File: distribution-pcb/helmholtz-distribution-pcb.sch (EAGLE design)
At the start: 34 parts

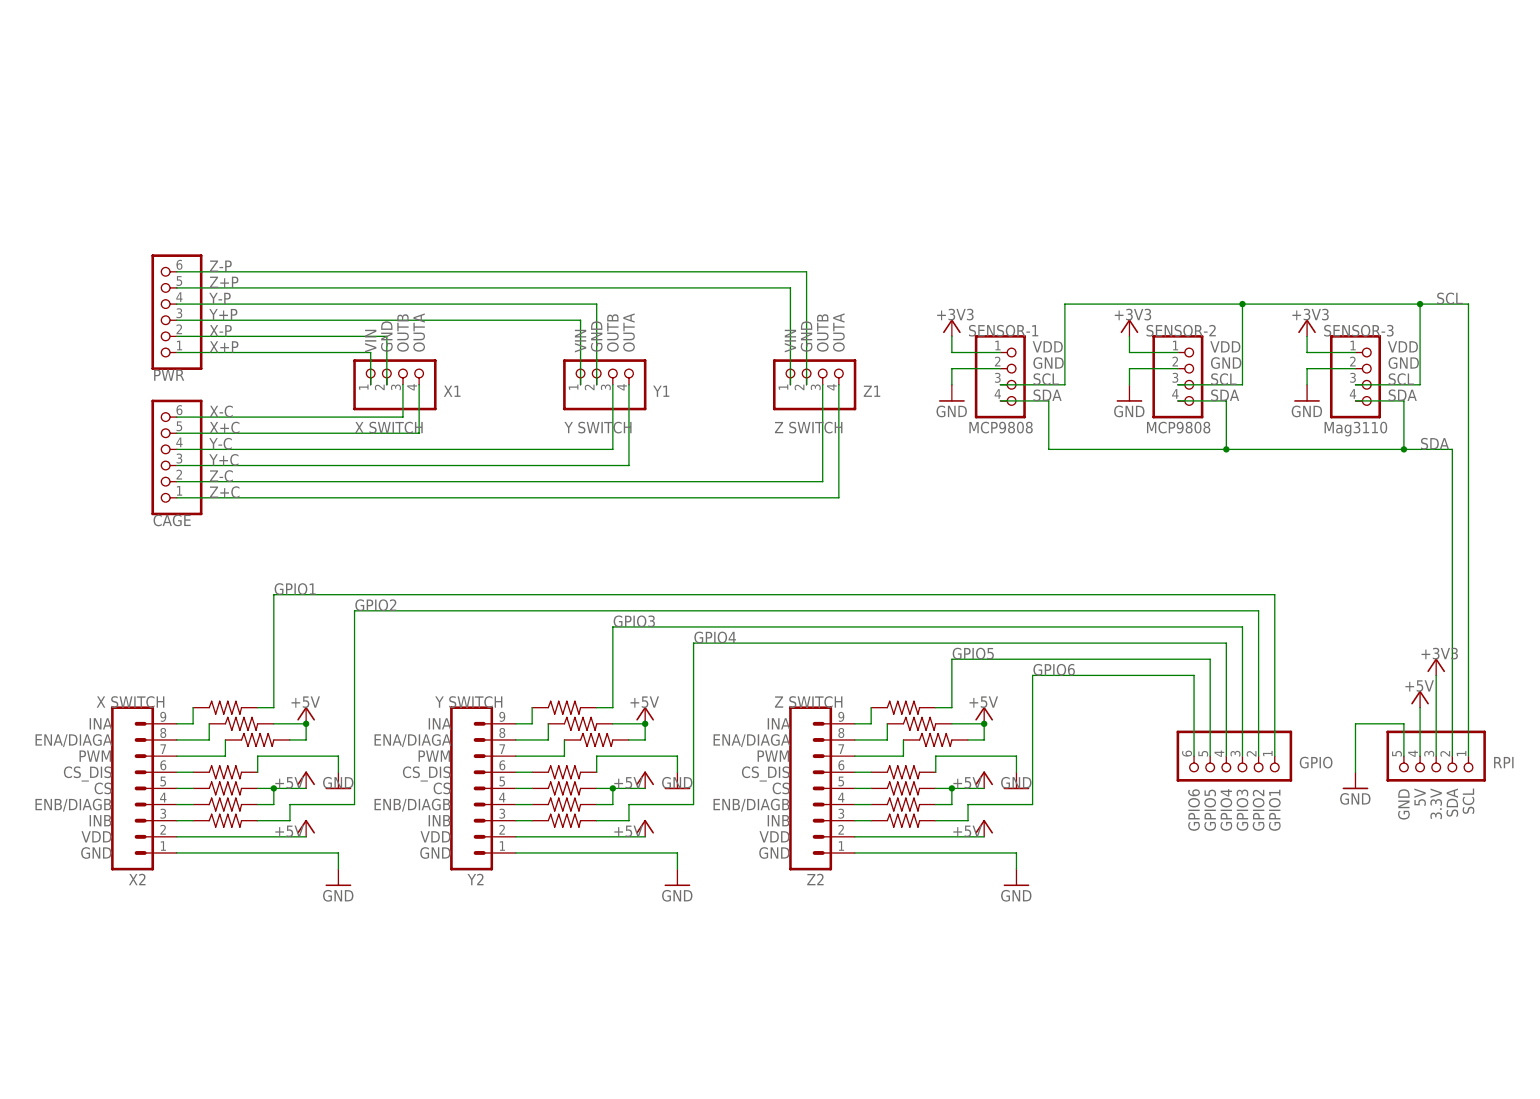
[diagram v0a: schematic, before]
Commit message: Latest distribution PCB design by Ceasar.
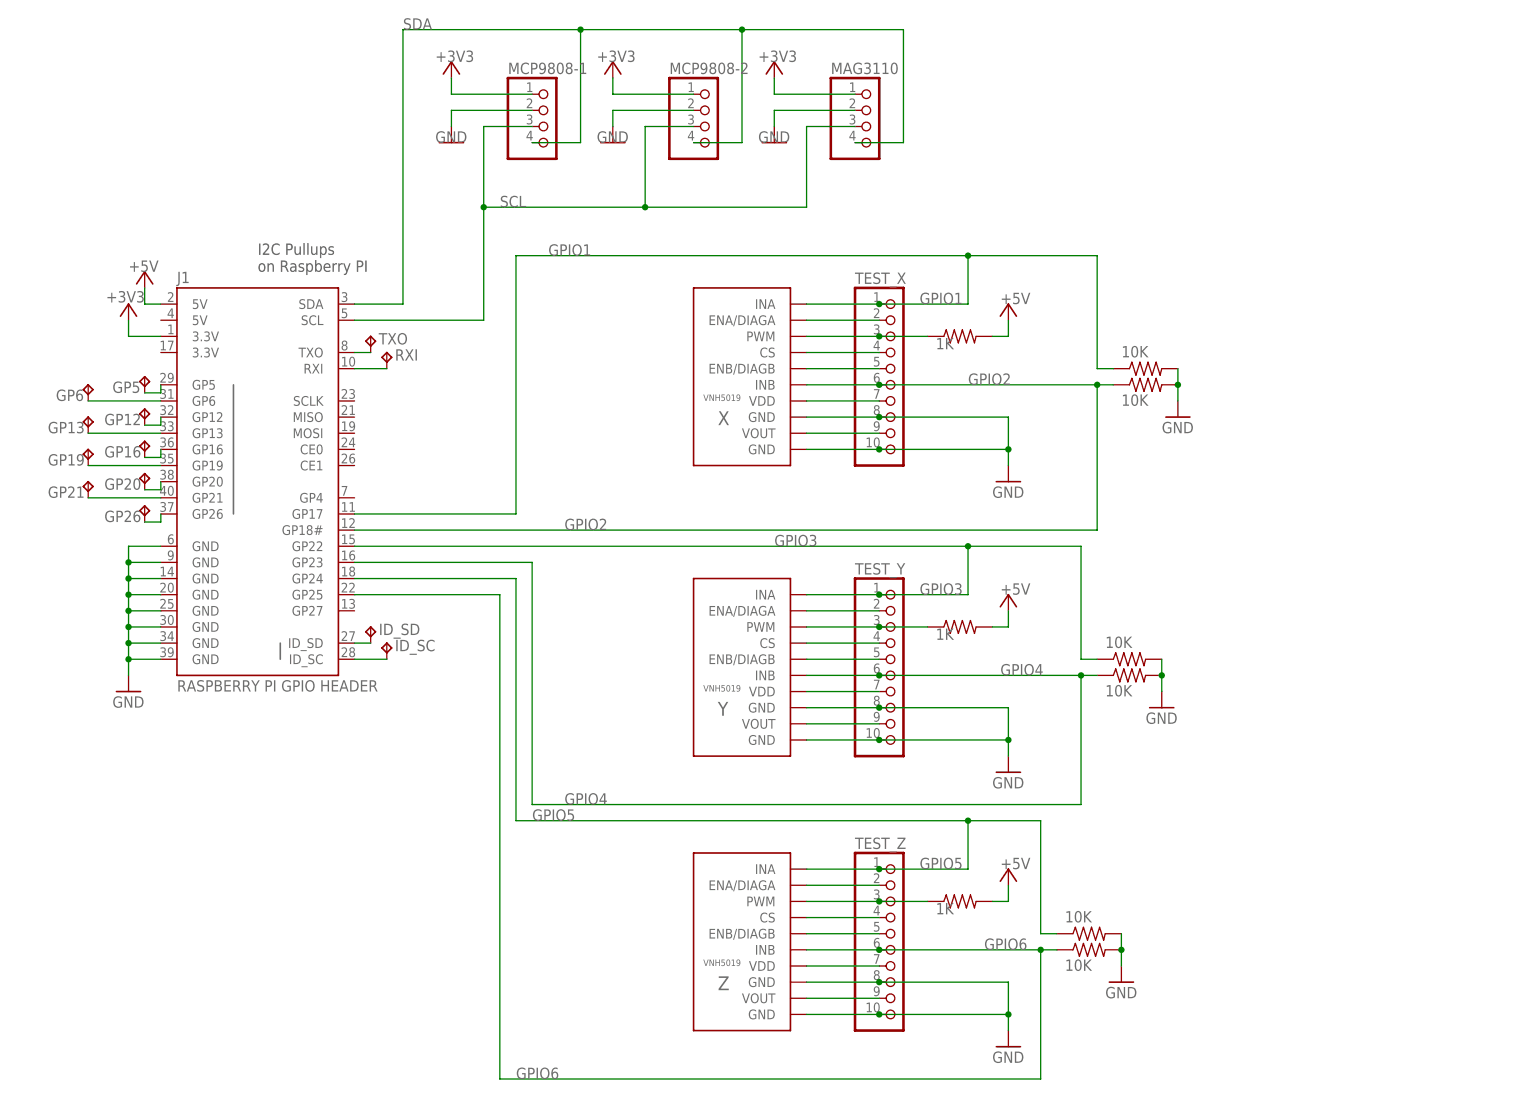
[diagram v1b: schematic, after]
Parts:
- removed CAGE, GPIO, PWR: (no value), pinhead:PINHD-1X6
- removed R1, R11, R12, R14, R15, R18, R19, R21, R4, R5, R6, R8: (no value), rcl:R-US_0204/7
- removed RPI: (no value), pinhead:PINHD-1X5
- removed SENSOR-1, SENSOR-2, SENSOR-3, X1, Y1, Z1: (no value), pinhead:PINHD-1X4
- removed X2, Y2, Z2: (no value), SparkFun-Connectors:CONN_09
- added GP12, GP13, GP16, GP19, GP20, GP21, GP26, GP5, GP6, ID_SC, ID_SD, RXI, TXO: TPPAD1-13, testpad:TPPAD1-13
- added J1: RASPBERRYPI-40-PIN-GPIO_PTH, SparkFun-Connectors:RASPBERRYPI-40-PIN-GPIO_PTH
- added MAG3110, MCP9808-1, MCP9808-2: (no value), pinhead:PINHD-1X4
- added TEST_X, TEST_Y, TEST_Z: (no value), pinhead:PINHD-1X10
- added X, Y, Z: VNH5019, HelmholtzCage:VNH5019
- R10, R16, R17, R2, R3, R9: value (none) -> 10K; device rcl:R-US_0204/7 -> rcl:R-US_R0603
- R13, R20, R7: value (none) -> 1K; device rcl:R-US_0204/7 -> rcl:R-US_R0603
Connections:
- removed net CSX: R7.1, X2.5
- removed net CSY: R8.1, Y2.5
- removed net CSZ: R21.1, Z2.5
- removed net DISX: R6.1, X2.6
- removed net DISY: R9.1, Y2.6
- removed net DISZ: R20.1, Z2.6
- removed net ENAX: R3.1, X2.8
- removed net ENAY: R12.1, Y2.8
- removed net ENAZ: R17.1, Z2.8
- removed net ENBX: R4.1, X2.4
- removed net ENBY: R11.1, Y2.4
- removed net ENBZ: R18.1, Z2.4
- removed net PWMX: R5.1, X2.7
- removed net PWMY: R10.1, Y2.7
- removed net PWMZ: R19.1, Z2.7
- removed net RGP1: R1.1, X2.9
- removed net RGP2: R2.1, X2.3
- removed net RGP3: R14.1, Y2.9
- removed net RGP4: R13.1, Y2.3
- removed net RGP5: R15.1, Z2.9
- removed net RGP6: R16.1, Z2.3
- removed net X+C: CAGE.5, X1.4
- removed net X+P: PWR.1, X1.1
- removed net X-C: CAGE.6, X1.3
- removed net X-P: PWR.2, X1.2
- removed net Y+C: CAGE.3, Y1.4
- removed net Y+P: PWR.3, Y1.1
- removed net Y-C: CAGE.4, Y1.3
- removed net Y-P: PWR.4, Y1.2
- removed net Z+C: CAGE.1, Z1.4
- removed net Z+P: PWR.5, Z1.1
- removed net Z-C: CAGE.2, Z1.3
- removed net Z-P: PWR.6, Z1.2
- new net CS_X: TEST_X.4, X.CS
- new net CS_Y: TEST_Y.4, Y.CS
- new net CS_Z: TEST_Z.4, Z.CS
- new net ENA/DIAGA_X: TEST_X.2, X.ENA/DIAGA
- new net ENA/DIAGA_Y: TEST_Y.2, Y.ENA/DIAGA
- new net ENA/DIAGA_Z: TEST_Z.2, Z.ENA/DIAGA
- new net ENB/DIAGB_X: TEST_X.5, X.ENB/DIAGB
- new net ENB/DIAGB_Y: TEST_Y.5, Y.ENB/DIAGB
- new net ENB/DIAGB_Z: TEST_Z.5, Z.ENB/DIAGB
- new net N$1: GP26.TP, J1.GP26
- new net N$10: J1.TXO, TXO.TP
- new net N$11: J1.RXI, RXI.TP
- new net N$12: ID_SD.TP, J1.ID_SD
- new net N$13: ID_SC.TP, J1.ID_SC
- new net N$2: GP21.TP, J1.GP21
- new net N$3: GP20.TP, J1.GP20
- new net N$4: GP19.TP, J1.GP19
- new net N$5: GP16.TP, J1.GP16
- new net N$6: GP13.TP, J1.GP13
- new net N$7: GP12.TP, J1.GP12
- new net N$8: GP6.TP, J1.GP6
- new net N$9: GP5.TP, J1.GP5
- new net PWM_X: R20.1, TEST_X.3, X.PWM
- new net PWM_Y: R13.1, TEST_Y.3, Y.PWM
- new net PWM_Z: R7.1, TEST_Z.3, Z.PWM
- new net VDD_X: TEST_X.7, X.VDD
- new net VDD_Y: TEST_Y.7, Y.VDD
- new net VDD_Z: TEST_Z.7, Z.VDD
- new net VOUT_X: TEST_X.9, X.VOUT
- new net VOUT_Y: TEST_Y.9, Y.VOUT
- new net VOUT_Z: TEST_Z.9, Z.VOUT
- net +3V3: now also J1.3.3V@1, MAG3110.1, MCP9808-1.1, MCP9808-2.1; no longer RPI.3, SENSOR-1.1, SENSOR-2.1, SENSOR-3.1
- net +5V: now also J1.5V@2, R13.2, R20.2; no longer R10.2, R11.2, R12.2, R17.2, R18.2, R19.2, R21.2, R3.2, R4.2, R5.2, R8.2, RPI.4, X2.2, Y2.2, Z2.2
- net GND: now also J1.GND@14, J1.GND@20, J1.GND@25, J1.GND@30, J1.GND@34, J1.GND@39, J1.GND@6, J1.GND@9, MAG3110.2, MCP9808-1.2, MCP9808-2.2, R10.2, R16.2, R17.2, R2.2, R3.2, TEST_X.10, TEST_X.8, TEST_Y.10, TEST_Y.8, TEST_Z.10, TEST_Z.8, X.GND@1, X.GND@2, Y.GND@1, Y.GND@2, Z.GND@1, Z.GND@2; no longer R20.2, R6.2, RPI.5, SENSOR-1.2, SENSOR-2.2, SENSOR-3.2, X2.1, Y2.1, Z2.1
- net GPIO1: now also J1.GP17, R17.1, TEST_X.1, X.INA; no longer GPIO.1, R1.2
- net GPIO2: now also J1.GP18#, R16.1, TEST_X.6, X.INB; no longer GPIO.2, R2.2
- net GPIO3: now also J1.GP22, R10.1, TEST_Y.1, Y.INA; no longer GPIO.3, R14.2
- net GPIO4: now also J1.GP23, R9.1, TEST_Y.6, Y.INB; no longer GPIO.4, R13.2
- net GPIO5: now also J1.GP24, R3.1, TEST_Z.1, Z.INA; no longer GPIO.5, R15.2
- net GPIO6: now also J1.GP25, R2.1, TEST_Z.6, Z.INB; no longer GPIO.6, R16.2
- net SCL: now also J1.SCL, MAG3110.3, MCP9808-1.3, MCP9808-2.3; no longer RPI.1, SENSOR-1.3, SENSOR-2.3, SENSOR-3.3
- net SDA: now also J1.SDA, MAG3110.4, MCP9808-1.4, MCP9808-2.4; no longer RPI.2, SENSOR-1.4, SENSOR-2.4, SENSOR-3.4
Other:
- note added: "I2C Pullups on Raspberry PI"
- note added: "RASPBERRY PI GPIO HEADER"
- note added: "X"
- note added: "Y"
- note added: "Z"
- note removed: "3.3V"
- note removed: "5V"
- note removed: "CS"
- note removed: "CS_DIS"
- note removed: "ENA/DIAGA"
- note removed: "ENB/DIAGB"
- note removed: "GND"
- note removed: "GPIO1"
- note removed: "GPIO2"
- note removed: "GPIO3"
- note removed: "GPIO4"
- note removed: "GPIO5"
- note removed: "GPIO6"
- note removed: "INA"
- note removed: "INB"
- note removed: "MCP9808"
- note removed: "Mag3110"
- note removed: "OUTA"
- note removed: "OUTB"
- note removed: "PWM"
- note removed: "SCL"
- note removed: "SDA"
- note removed: "VDD"
- note removed: "VIN"
- note removed: "X SWITCH"
- note removed: "Y SWITCH"
- note removed: "Z SWITCH"

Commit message: Added mounting holes to VNH boards, put mounting holes on board, and changed font to vector.
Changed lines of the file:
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@@
 <setting verticaltext="up"/>
 </settings>
-<grid distance="0.05" unitdist="inch" unit="inch" style="lines" multiple="2" display="no" altdistance="0.01" altunitdist="inch" altunit="inch"/>
+<grid distance="0.1" unitdist="inch" unit="inch" style="lines" multiple="1" display="no" altdistance="0.01" altunitdist="inch" altunit="inch"/>
 <layers>
 <layer number="1" name="Top" color="4" fill="1" visible="no" active="no"/>
@@
 <pinref part="Z" gate="G$1" pin="GND@2"/>
 <pinref part="TEST_Z" gate="A" pin="10"/>
-<wire x1="152.4" y1="38.1" x2="163.83" y2="38.1" width="0.1524" layer="91"/>
+<wire x1="154.94" y1="38.1" x2="163.83" y2="38.1" width="0.1524" layer="91"/>
 <pinref part="Z" gate="G$1" pin="GND@1"/>
 <pinref part="TEST_Z" gate="A" pin="8"/>
-<wire x1="152.4" y1="43.18" x2="163.83" y2="43.18" width="0.1524" layer="91"/>
+<wire x1="154.94" y1="43.18" x2="163.83" y2="43.18" width="0.1524" layer="91"/>
 <pinref part="GND1" gate="1" pin="GND"/>
 <wire x1="184.15" y1="43.18" x2="184.15" y2="38.1" width="0.1524" layer="91"/>
@@
 <pinref part="Y" gate="G$1" pin="GND@2"/>
 <pinref part="TEST_Y" gate="A" pin="10"/>
-<wire x1="152.4" y1="81.28" x2="163.83" y2="81.28" width="0.1524" layer="91"/>
+<wire x1="154.94" y1="81.28" x2="163.83" y2="81.28" width="0.1524" layer="91"/>
 <pinref part="Y" gate="G$1" pin="GND@1"/>
 <pinref part="TEST_Y" gate="A" pin="8"/>
-<wire x1="152.4" y1="86.36" x2="163.83" y2="86.36" width="0.1524" layer="91"/>
+<wire x1="154.94" y1="86.36" x2="163.83" y2="86.36" width="0.1524" layer="91"/>
 <pinref part="GND2" gate="1" pin="GND"/>
 <wire x1="184.15" y1="86.36" x2="184.15" y2="81.28" width="0.1524" layer="91"/>
@@
 <pinref part="X" gate="G$1" pin="GND@1"/>
 <pinref part="TEST_X" gate="A" pin="8"/>
-<wire x1="152.4" y1="132.08" x2="163.83" y2="132.08" width="0.1524" layer="91"/>
+<wire x1="154.94" y1="132.08" x2="163.83" y2="132.08" width="0.1524" layer="91"/>
 <pinref part="X" gate="G$1" pin="GND@2"/>
 <pinref part="TEST_X" gate="A" pin="10"/>
-<wire x1="152.4" y1="127" x2="163.83" y2="127" width="0.1524" layer="91"/>
+<wire x1="154.94" y1="127" x2="163.83" y2="127" width="0.1524" layer="91"/>
 <pinref part="GND3" gate="1" pin="GND"/>
 <wire x1="184.15" y1="132.08" x2="184.15" y2="127" width="0.1524" layer="91"/>
@@
 <pinref part="Y" gate="G$1" pin="INA"/>
 <pinref part="TEST_Y" gate="A" pin="1"/>
-<wire x1="152.4" y1="104.14" x2="163.83" y2="104.14" width="0.1524" layer="91"/>
+<wire x1="154.94" y1="104.14" x2="163.83" y2="104.14" width="0.1524" layer="91"/>
 <wire x1="163.83" y1="104.14" x2="177.8" y2="104.14" width="0.1524" layer="91"/>
 <wire x1="177.8" y1="104.14" x2="177.8" y2="111.76" width="0.1524" layer="91"/>
@@
 <pinref part="Z" gate="G$1" pin="INA"/>
 <pinref part="TEST_Z" gate="A" pin="1"/>
-<wire x1="152.4" y1="60.96" x2="163.83" y2="60.96" width="0.1524" layer="91"/>
+<wire x1="154.94" y1="60.96" x2="163.83" y2="60.96" width="0.1524" layer="91"/>
 <wire x1="163.83" y1="60.96" x2="177.8" y2="60.96" width="0.1524" layer="91"/>
 <wire x1="177.8" y1="60.96" x2="177.8" y2="68.58" width="0.1524" layer="91"/>
@@
 <pinref part="Z" gate="G$1" pin="INB"/>
 <pinref part="TEST_Z" gate="A" pin="6"/>
-<wire x1="152.4" y1="48.26" x2="163.83" y2="48.26" width="0.1524" layer="91"/>
+<wire x1="154.94" y1="48.26" x2="163.83" y2="48.26" width="0.1524" layer="91"/>
 <wire x1="163.83" y1="48.26" x2="189.23" y2="48.26" width="0.1524" layer="91"/>
 <junction x="163.83" y="48.26"/>
@@
 <pinref part="X" gate="G$1" pin="INA"/>
 <pinref part="TEST_X" gate="A" pin="1"/>
-<wire x1="152.4" y1="149.86" x2="163.83" y2="149.86" width="0.1524" layer="91"/>
+<wire x1="154.94" y1="149.86" x2="163.83" y2="149.86" width="0.1524" layer="91"/>
 <wire x1="163.83" y1="149.86" x2="177.8" y2="149.86" width="0.1524" layer="91"/>
 <wire x1="177.8" y1="149.86" x2="177.8" y2="157.48" width="0.1524" layer="91"/>
@@
 <pinref part="X" gate="G$1" pin="INB"/>
 <pinref part="TEST_X" gate="A" pin="6"/>
-<wire x1="152.4" y1="137.16" x2="163.83" y2="137.16" width="0.1524" layer="91"/>
+<wire x1="154.94" y1="137.16" x2="163.83" y2="137.16" width="0.1524" layer="91"/>
 <wire x1="163.83" y1="137.16" x2="198.12" y2="137.16" width="0.1524" layer="91"/>
 <junction x="163.83" y="137.16"/>
@@
 <label x="182.88" y="91.44" size="1.778" layer="95"/>
 <pinref part="Y" gate="G$1" pin="INB"/>
-<wire x1="152.4" y1="91.44" x2="163.83" y2="91.44" width="0.1524" layer="91"/>
+<wire x1="154.94" y1="91.44" x2="163.83" y2="91.44" width="0.1524" layer="91"/>
 <wire x1="163.83" y1="91.44" x2="195.58" y2="91.44" width="0.1524" layer="91"/>
 <junction x="163.83" y="91.44"/>
@@
 <pinref part="X" gate="G$1" pin="ENA/DIAGA"/>
 <pinref part="TEST_X" gate="A" pin="2"/>
-<wire x1="152.4" y1="147.32" x2="163.83" y2="147.32" width="0.1524" layer="91"/>
+<wire x1="154.94" y1="147.32" x2="163.83" y2="147.32" width="0.1524" layer="91"/>
 </segment>
 </net>
@@
 <pinref part="X" gate="G$1" pin="PWM"/>
 <pinref part="TEST_X" gate="A" pin="3"/>
-<wire x1="152.4" y1="144.78" x2="163.83" y2="144.78" width="0.1524" layer="91"/>
+<wire x1="154.94" y1="144.78" x2="163.83" y2="144.78" width="0.1524" layer="91"/>
 <pinref part="R20" gate="G$1" pin="1"/>
 <wire x1="163.83" y1="144.78" x2="171.45" y2="144.78" width="0.1524" layer="91"/>
@@
 <pinref part="X" gate="G$1" pin="CS"/>
 <pinref part="TEST_X" gate="A" pin="4"/>
-<wire x1="152.4" y1="142.24" x2="163.83" y2="142.24" width="0.1524" layer="91"/>
+<wire x1="154.94" y1="142.24" x2="163.83" y2="142.24" width="0.1524" layer="91"/>
 </segment>
 </net>
@@
 <pinref part="X" gate="G$1" pin="ENB/DIAGB"/>
 <pinref part="TEST_X" gate="A" pin="5"/>
-<wire x1="152.4" y1="139.7" x2="163.83" y2="139.7" width="0.1524" layer="91"/>
+<wire x1="154.94" y1="139.7" x2="163.83" y2="139.7" width="0.1524" layer="91"/>
 </segment>
 </net>
@@
 <pinref part="X" gate="G$1" pin="VDD"/>
 <pinref part="TEST_X" gate="A" pin="7"/>
-<wire x1="152.4" y1="134.62" x2="163.83" y2="134.62" width="0.1524" layer="91"/>
+<wire x1="154.94" y1="134.62" x2="163.83" y2="134.62" width="0.1524" layer="91"/>
 </segment>
 </net>
@@
 <pinref part="Z" gate="G$1" pin="VOUT"/>
 <pinref part="TEST_Z" gate="A" pin="9"/>
-<wire x1="152.4" y1="40.64" x2="163.83" y2="40.64" width="0.1524" layer="91"/>
+<wire x1="154.94" y1="40.64" x2="163.83" y2="40.64" width="0.1524" layer="91"/>
 </segment>
 </net>
@@
 <pinref part="Y" gate="G$1" pin="VOUT"/>
 <pinref part="TEST_Y" gate="A" pin="9"/>
-<wire x1="152.4" y1="83.82" x2="163.83" y2="83.82" width="0.1524" layer="91"/>
+<wire x1="154.94" y1="83.82" x2="163.83" y2="83.82" width="0.1524" layer="91"/>
 </segment>
 </net>
@@
 <pinref part="X" gate="G$1" pin="VOUT"/>
 <pinref part="TEST_X" gate="A" pin="9"/>
-<wire x1="152.4" y1="129.54" x2="163.83" y2="129.54" width="0.1524" layer="91"/>
+<wire x1="154.94" y1="129.54" x2="163.83" y2="129.54" width="0.1524" layer="91"/>
 </segment>
 </net>
@@
 <pinref part="Y" gate="G$1" pin="ENA/DIAGA"/>
 <pinref part="TEST_Y" gate="A" pin="2"/>
-<wire x1="152.4" y1="101.6" x2="163.83" y2="101.6" width="0.1524" layer="91"/>
+<wire x1="154.94" y1="101.6" x2="163.83" y2="101.6" width="0.1524" layer="91"/>
 </segment>
 </net>
@@
 <pinref part="Y" gate="G$1" pin="PWM"/>
 <pinref part="TEST_Y" gate="A" pin="3"/>
-<wire x1="152.4" y1="99.06" x2="163.83" y2="99.06" width="0.1524" layer="91"/>
+<wire x1="154.94" y1="99.06" x2="163.83" y2="99.06" width="0.1524" layer="91"/>
 <pinref part="R13" gate="G$1" pin="1"/>
 <wire x1="163.83" y1="99.06" x2="171.45" y2="99.06" width="0.1524" layer="91"/>
@@
 <pinref part="Y" gate="G$1" pin="CS"/>
 <pinref part="TEST_Y" gate="A" pin="4"/>
-<wire x1="152.4" y1="96.52" x2="163.83" y2="96.52" width="0.1524" layer="91"/>
+<wire x1="154.94" y1="96.52" x2="163.83" y2="96.52" width="0.1524" layer="91"/>
 </segment>
 </net>
@@
 <pinref part="Y" gate="G$1" pin="ENB/DIAGB"/>
 <pinref part="TEST_Y" gate="A" pin="5"/>
-<wire x1="152.4" y1="93.98" x2="163.83" y2="93.98" width="0.1524" layer="91"/>
+<wire x1="154.94" y1="93.98" x2="163.83" y2="93.98" width="0.1524" layer="91"/>
 </segment>
 </net>
@@
 <pinref part="Y" gate="G$1" pin="VDD"/>
 <pinref part="TEST_Y" gate="A" pin="7"/>
-<wire x1="152.4" y1="88.9" x2="163.83" y2="88.9" width="0.1524" layer="91"/>
+<wire x1="154.94" y1="88.9" x2="163.83" y2="88.9" width="0.1524" layer="91"/>
 </segment>
 </net>
@@
 <pinref part="Z" gate="G$1" pin="ENA/DIAGA"/>
 <pinref part="TEST_Z" gate="A" pin="2"/>
-<wire x1="152.4" y1="58.42" x2="163.83" y2="58.42" width="0.1524" layer="91"/>
+<wire x1="154.94" y1="58.42" x2="163.83" y2="58.42" width="0.1524" layer="91"/>
 </segment>
 </net>
@@
 <pinref part="Z" gate="G$1" pin="CS"/>
 <pinref part="TEST_Z" gate="A" pin="4"/>
-<wire x1="152.4" y1="53.34" x2="163.83" y2="53.34" width="0.1524" layer="91"/>
+<wire x1="154.94" y1="53.34" x2="163.83" y2="53.34" width="0.1524" layer="91"/>
 </segment>
 </net>
@@
 <pinref part="Z" gate="G$1" pin="ENB/DIAGB"/>
 <pinref part="TEST_Z" gate="A" pin="5"/>
-<wire x1="152.4" y1="50.8" x2="163.83" y2="50.8" width="0.1524" layer="91"/>
+<wire x1="154.94" y1="50.8" x2="163.83" y2="50.8" width="0.1524" layer="91"/>
 </segment>
 </net>
@@
 <pinref part="Z" gate="G$1" pin="VDD"/>
 <pinref part="TEST_Z" gate="A" pin="7"/>
-<wire x1="152.4" y1="45.72" x2="163.83" y2="45.72" width="0.1524" layer="91"/>
+<wire x1="154.94" y1="45.72" x2="163.83" y2="45.72" width="0.1524" layer="91"/>
 </segment>
 </net>
@@
 <pinref part="Z" gate="G$1" pin="PWM"/>
 <pinref part="TEST_Z" gate="A" pin="3"/>
-<wire x1="152.4" y1="55.88" x2="163.83" y2="55.88" width="0.1524" layer="91"/>
+<wire x1="154.94" y1="55.88" x2="163.83" y2="55.88" width="0.1524" layer="91"/>
 <pinref part="R7" gate="G$1" pin="1"/>
 <wire x1="163.83" y1="55.88" x2="171.45" y2="55.88" width="0.1524" layer="91"/>
